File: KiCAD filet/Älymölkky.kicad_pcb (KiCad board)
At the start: 2 copper layers, 111 parts, among them P0.18_TP1 Conn_01x01_Male, U1 nRF52810-QCxx, X1 32MHz Crystal, X1_C1 12pF, X1_C2 12pF, X2 32.768 kHz Crystal, X2_C11 12pF, X2_C12 12pF

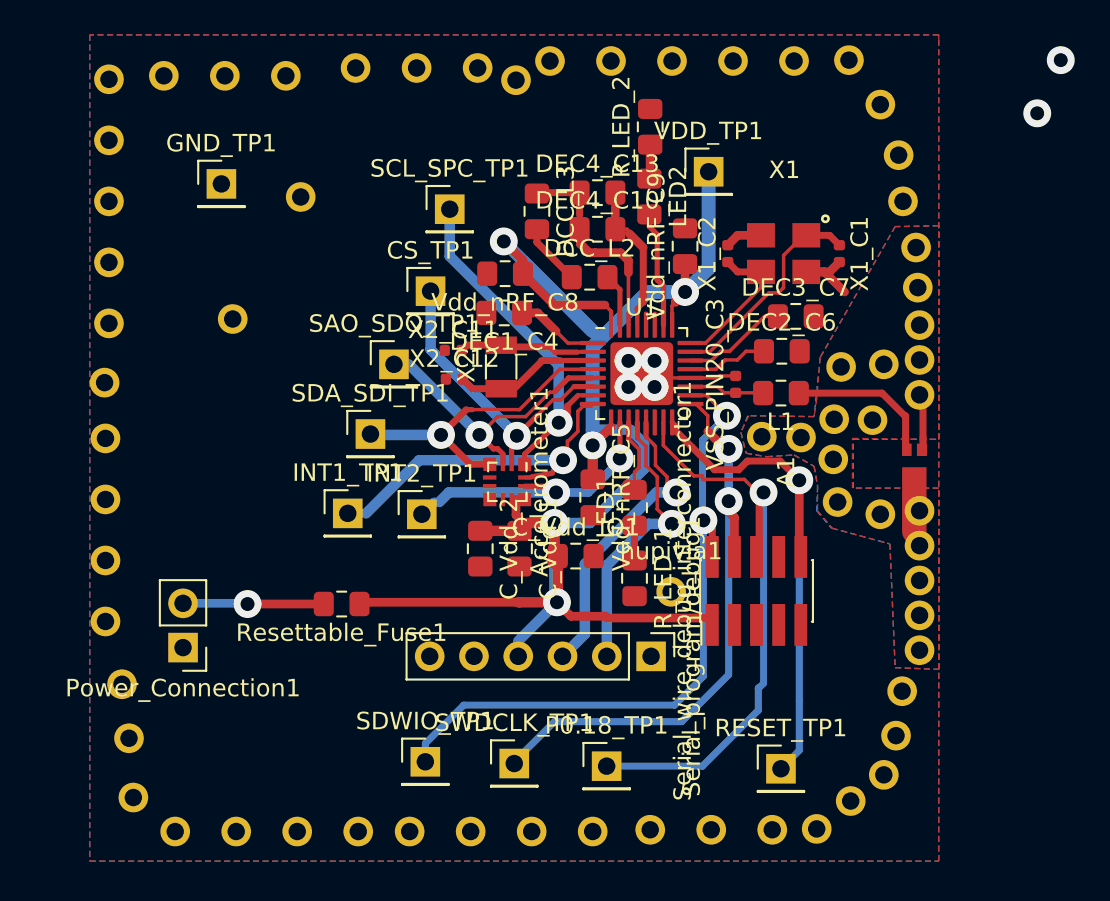
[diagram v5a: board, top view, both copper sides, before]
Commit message: Added switch, modified components to right sizes
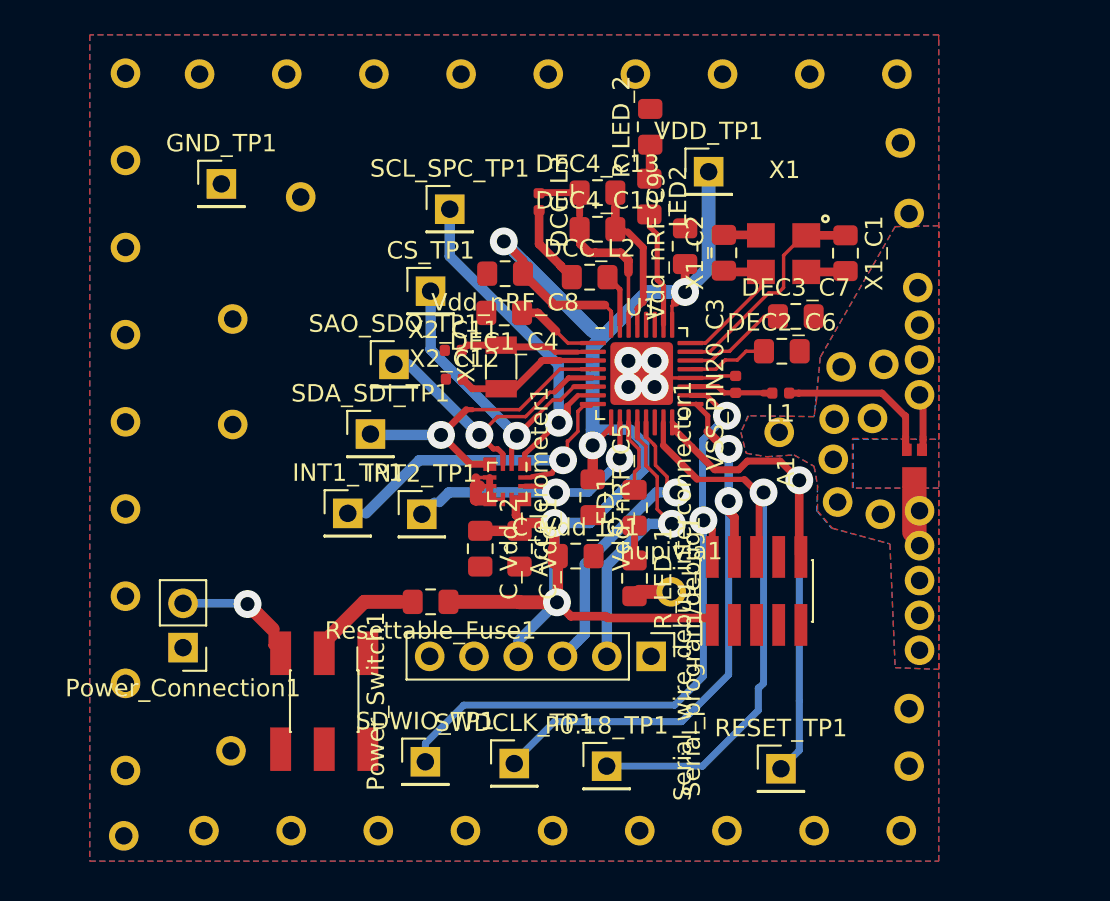
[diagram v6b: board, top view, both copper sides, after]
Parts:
- removed the ? at (101.0, 111.8)
- removed the ? at (100.0, 94.5)
- removed the ? at (100.0, 101.2)
- removed the ? at (104.0, 120.2)
- removed the ? at (107.5, 120.2)
- removed the ? at (111.0, 120.2)
- removed the ? at (114.5, 120.2)
- removed the ? at (100.0, 104.7)
- removed the ? at (117.5, 120.2)
- removed the ? at (121.0, 120.2)
- removed the ? at (124.5, 120.2)
- removed the ? at (128.0, 120.2)
- removed the ? at (100.0, 108.2)
- removed the ? at (131.3, 120.2)
- removed the ? at (134.8, 120.2)
- removed the ? at (138.3, 120.2)
- removed the ? at (140.8, 120.1)
- removed the ? at (100.2, 91.1)
- removed the ? at (142.7, 76.0)
- removed the ? at (100.2, 87.6)
- removed the ? at (125.5, 76.0)
- removed the ? at (144.5, 78.5)
- removed the ? at (100.2, 84.1)
- removed the ? at (100.2, 80.6)
- removed the ? at (121.4, 76.5)
- removed the ? at (117.9, 76.5)
- removed the ? at (114.4, 76.5)
- removed the ? at (145.6, 81.5)
- removed the ? at (100.2, 77.1)
- removed the ? at (110.4, 76.9)
- removed the ? at (106.9, 76.9)
- removed the ? at (129.1, 76.0)
- removed the ? at (103.4, 76.9)
- removed the ? at (145.8, 84.1)
- removed the ? at (145.4, 114.8)
- removed the ? at (123.6, 77.2)
- removed the ? at (142.8, 118.5)
- removed the ? at (137.7, 97.6)
- removed the ? at (132.6, 76.0)
- removed the ? at (146.6, 86.8)
- removed the ? at (139.9, 97.7)
- removed the ? at (101.4, 114.9)
- removed the ? at (136.1, 76.0)
- removed the ? at (139.6, 76.0)
- removed the ? at (100.0, 97.7)
- removed the ? at (101.7, 118.3)
- added ?: Conn_01x01_Male, Connector_PinHeader_2.54mm:PinHeader_1x01_P2.54mm_Vertical, F.Cu at (110.5, 76.8)
- added ?: Conn_01x01_Male, Connector_PinHeader_2.54mm:PinHeader_1x01_P2.54mm_Vertical, F.Cu at (101.2, 81.8)
- added ?: Conn_01x01_Male, Connector_PinHeader_2.54mm:PinHeader_1x01_P2.54mm_Vertical, F.Cu at (101.2, 76.8)
- added ?: Conn_01x01_Male, Connector_PinHeader_2.54mm:PinHeader_1x01_P2.54mm_Vertical, F.Cu at (101.2, 86.8)
- added ?: Conn_01x01_Male, Connector_PinHeader_2.54mm:PinHeader_1x01_P2.54mm_Vertical, F.Cu at (101.2, 91.8)
- added ?: Conn_01x01_Male, Connector_PinHeader_2.54mm:PinHeader_1x01_P2.54mm_Vertical, F.Cu at (101.2, 96.8)
- added ?: Conn_01x01_Male, Connector_PinHeader_2.54mm:PinHeader_1x01_P2.54mm_Vertical, F.Cu at (101.2, 101.8)
- added ?: Conn_01x01_Male, Connector_PinHeader_2.54mm:PinHeader_1x01_P2.54mm_Vertical, F.Cu at (101.2, 106.8)
- added ?: Conn_01x01_Male, Connector_PinHeader_2.54mm:PinHeader_1x01_P2.54mm_Vertical, F.Cu at (101.2, 111.8)
- added ?: Conn_01x01_Male, Connector_PinHeader_2.54mm:PinHeader_1x01_P2.54mm_Vertical, F.Cu at (101.2, 116.8)
- added ?: Conn_01x01_Male, Connector_PinHeader_2.54mm:PinHeader_1x01_P2.54mm_Vertical, F.Cu at (107.3, 96.9)
- added ?: Conn_01x01_Male, Connector_PinHeader_2.54mm:PinHeader_1x01_P2.54mm_Vertical, F.Cu at (105.5, 76.8)
- added ?: Conn_01x01_Male, Connector_PinHeader_2.54mm:PinHeader_1x01_P2.54mm_Vertical, F.Cu at (107.2, 115.6)
- added ?: Conn_01x01_Male, Connector_PinHeader_2.54mm:PinHeader_1x01_P2.54mm_Vertical, F.Cu at (101.1, 120.5)
- added ?: Conn_01x01_Male, Connector_PinHeader_2.54mm:PinHeader_1x01_P2.54mm_Vertical, F.Cu at (146.2, 116.5)
- added ?: Conn_01x01_Male, Connector_PinHeader_2.54mm:PinHeader_1x01_P2.54mm_Vertical, F.Cu at (145.7, 80.8)
- added ?: Conn_01x01_Male, Connector_PinHeader_2.54mm:PinHeader_1x01_P2.54mm_Vertical, F.Cu at (146.2, 84.8)
- added ?: Conn_01x01_Male, Connector_PinHeader_2.54mm:PinHeader_1x01_P2.54mm_Vertical, F.Cu at (145.7, 120.2)
- added ?: Conn_01x01_Male, Connector_PinHeader_2.54mm:PinHeader_1x01_P2.54mm_Vertical, F.Cu at (140.7, 120.2)
- added ?: Conn_01x01_Male, Connector_PinHeader_2.54mm:PinHeader_1x01_P2.54mm_Vertical, F.Cu at (135.7, 120.2)
- added ?: Conn_01x01_Male, Connector_PinHeader_2.54mm:PinHeader_1x01_P2.54mm_Vertical, F.Cu at (130.7, 120.2)
- added ?: Conn_01x01_Male, Connector_PinHeader_2.54mm:PinHeader_1x01_P2.54mm_Vertical, F.Cu at (125.7, 120.2)
- added ?: Conn_01x01_Male, Connector_PinHeader_2.54mm:PinHeader_1x01_P2.54mm_Vertical, F.Cu at (125.5, 76.8)
- added ?: Conn_01x01_Male, Connector_PinHeader_2.54mm:PinHeader_1x01_P2.54mm_Vertical, F.Cu at (120.7, 120.2)
- added ?: Conn_01x01_Male, Connector_PinHeader_2.54mm:PinHeader_1x01_P2.54mm_Vertical, F.Cu at (115.7, 120.2)
- added ?: Conn_01x01_Male, Connector_PinHeader_2.54mm:PinHeader_1x01_P2.54mm_Vertical, F.Cu at (110.7, 120.2)
- added ?: Conn_01x01_Male, Connector_PinHeader_2.54mm:PinHeader_1x01_P2.54mm_Vertical, F.Cu at (140.4, 76.8)
- added ?: Conn_01x01_Male, Connector_PinHeader_2.54mm:PinHeader_1x01_P2.54mm_Vertical, F.Cu at (138.7, 97.3)
- added ?: Conn_01x01_Male, Connector_PinHeader_2.54mm:PinHeader_1x01_P2.54mm_Vertical, F.Cu at (115.5, 76.8)
- added ?: Conn_01x01_Male, Connector_PinHeader_2.54mm:PinHeader_1x01_P2.54mm_Vertical, F.Cu at (120.5, 76.8)
- added ?: Conn_01x01_Male, Connector_PinHeader_2.54mm:PinHeader_1x01_P2.54mm_Vertical, F.Cu at (135.4, 76.8)
- added ?: Conn_01x01_Male, Connector_PinHeader_2.54mm:PinHeader_1x01_P2.54mm_Vertical, F.Cu at (145.4, 76.8)
- added ?: Conn_01x01_Male, Connector_PinHeader_2.54mm:PinHeader_1x01_P2.54mm_Vertical, F.Cu at (130.4, 76.8)
- added Power_Switch1: Conn_02x03_Odd_Even, Connector_PinHeader_1.27mm:PinHeader_2x03_P1.27mm_Vertical_SMD, F.Cu at (112.6, 112.8)
- DCC_L3: footprint Capacitor_SMD:C_0805_2012Metric_Pad1.15x1.40mm_HandSolder -> Capacitor_SMD:C_0402_1005Metric
- L1: footprint Resistor_SMD:R_0805_2012Metric_Pad1.15x1.40mm_HandSolder -> Resistor_SMD:R_0402_1005Metric
- X1_C1, X1_C2: footprint Capacitor_SMD:C_0402_1005Metric -> Capacitor_SMD:C_0805_2012Metric_Pad1.15x1.40mm_HandSolder
- moved ? 39.1 mm to (105.7, 120.2)
- moved Resettable_Fuse1 5.10 mm to (118.7, 107.1)
- moved ? 1.08 mm to (146.2, 113.2)
- moved DCC_L3 0.56 mm to (124.9, 84.1)
- moved X1_C1 0.35 mm to (142.5, 87.1)
- moved X1_C2 0.23 mm to (135.5, 87.0)
- moved ? 0.10 mm to (144.1, 96.5)
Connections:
- Resettable_Fuse1 pad 2: Net-(Power_Connection1-Pad2) -> Net-(Power_Switch1-Pad3)
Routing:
- net Net-(Power_Switch1-Pad3): track 0.00 -> 6.68 mm
- net Earth: track 25.7 -> 30.9 mm
- net VDD: track 97.9 -> 92.8 mm
- net Net-(DCC_L2-Pad1): track 3.58 -> 4.62 mm
- net Net-(Power_Connection1-Pad2): track 8.09 -> 7.33 mm
- net /ANTENNA: track 8.40 -> 8.96 mm
- net Net-(L1-Pad2): track 4.32 -> 4.84 mm
- net (no net): vias 2 -> 0
